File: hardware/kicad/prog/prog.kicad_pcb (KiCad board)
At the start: 4 copper layers, 174 x 134 mm, 144 parts, among them J1 AES_PROG, J2 Câble PROG-CHA, J3 CONF P, J4 CONF V, J5 microSD, SW1 Retour menu, U1 AMS1117-3.3, U10 iCE40HX4K-TQ144, U11 W9825G6KH-6, U12 iCE40HX4K-TQ144, U13 W9825G6KH-6, U2 AP2112K-1.2, U3 74LVC16244A, U4 74LVC16244A, U5 74LVC16244A, U6 74LVC16245A, U7 74LVC16245A, U8 74AHCT125, U9 74LVC1G07, X1 25 MHz 3,3 V, X2 25 MHz 3,3 V

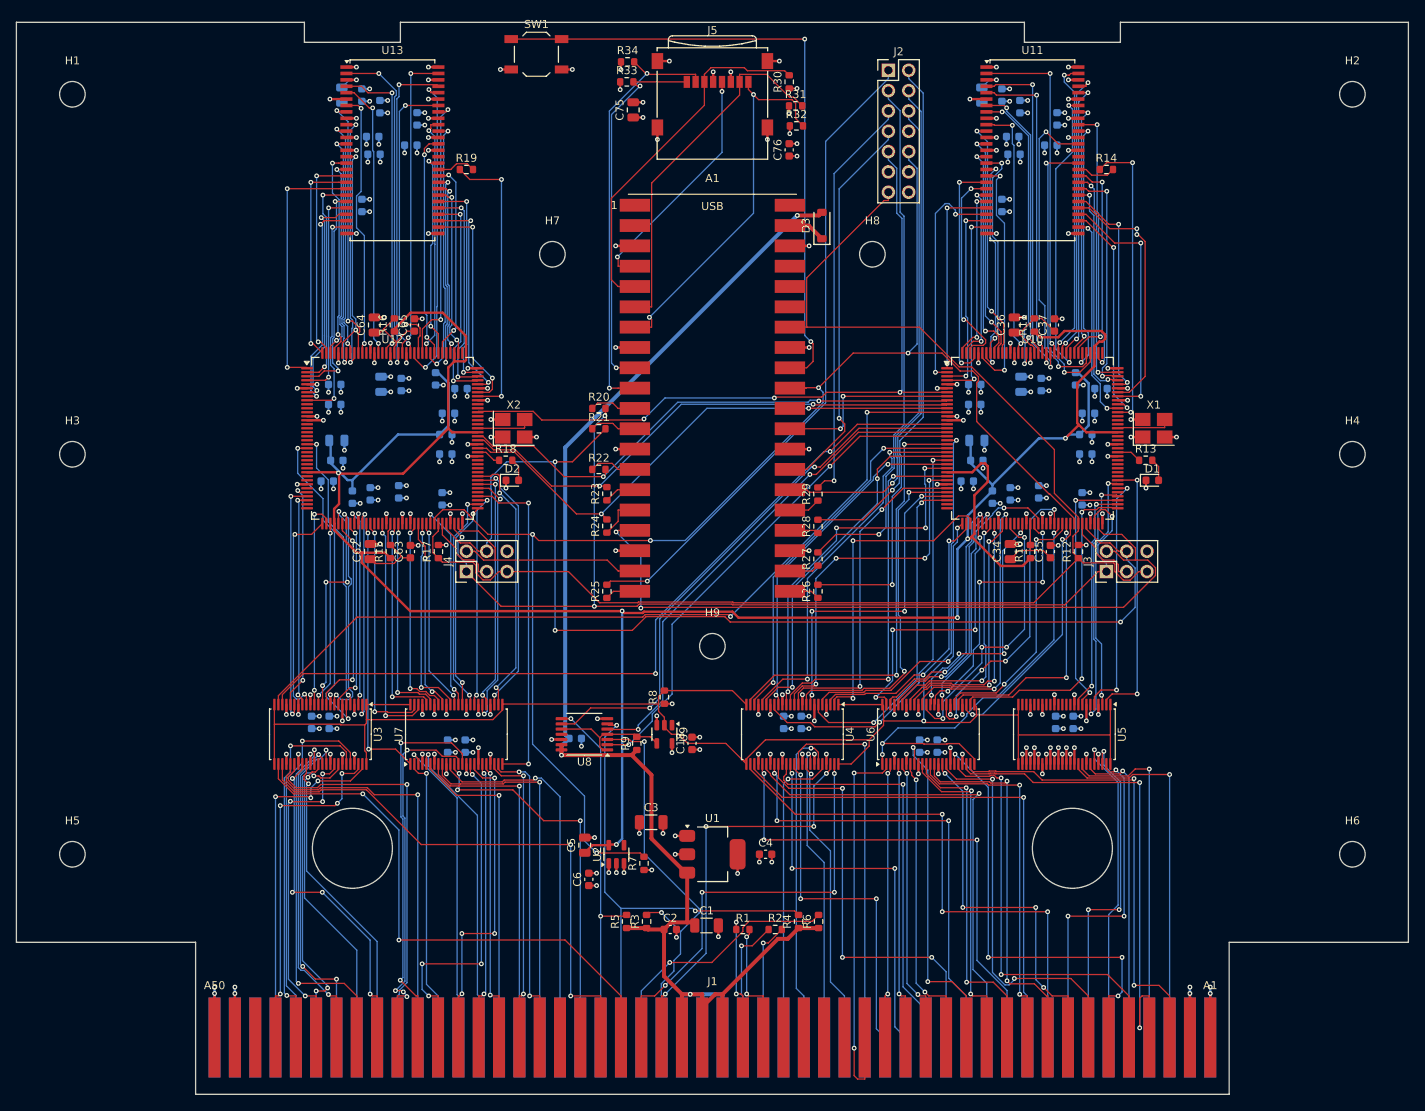
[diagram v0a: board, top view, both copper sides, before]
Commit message: Régulateur 3,3 V à découpage, horloge SDRAM adaptée côté FPGA, U8 en 74AHCT125
- AP63203 (TSOT-23-6, sortie fixe 3,3 V, ~90 %) à la place de
  l'AMS1117 : ~0,15 W de pertes au lieu de ~0,75 W et moins de courant
  tiré sur le 5 V de la console ; L 4,7 µH, Cin 10 µF, Cout 2 x 22 µF.
- Résistance série de 33 ohms de l'horloge SDRAM déclarée avec le FPGA :
  placée à 2,7 mm de sa broche (au lieu de ~30 mm, côté SDRAM).
- CHA : U8 (16244 pour 2 canaux) remplacé par un 74AHCT125.
Cartes replacées, contrôle Freerouting sans violation ; routage des
deux cartes et vérification de timing en cours.

Co-Authored-By: Claude Opus 5.5 <noreply@anthropic.com>
Claude-Session: https://claude.ai/code/session_01WKfXP1YJ8otGxZ5dsY6Agh
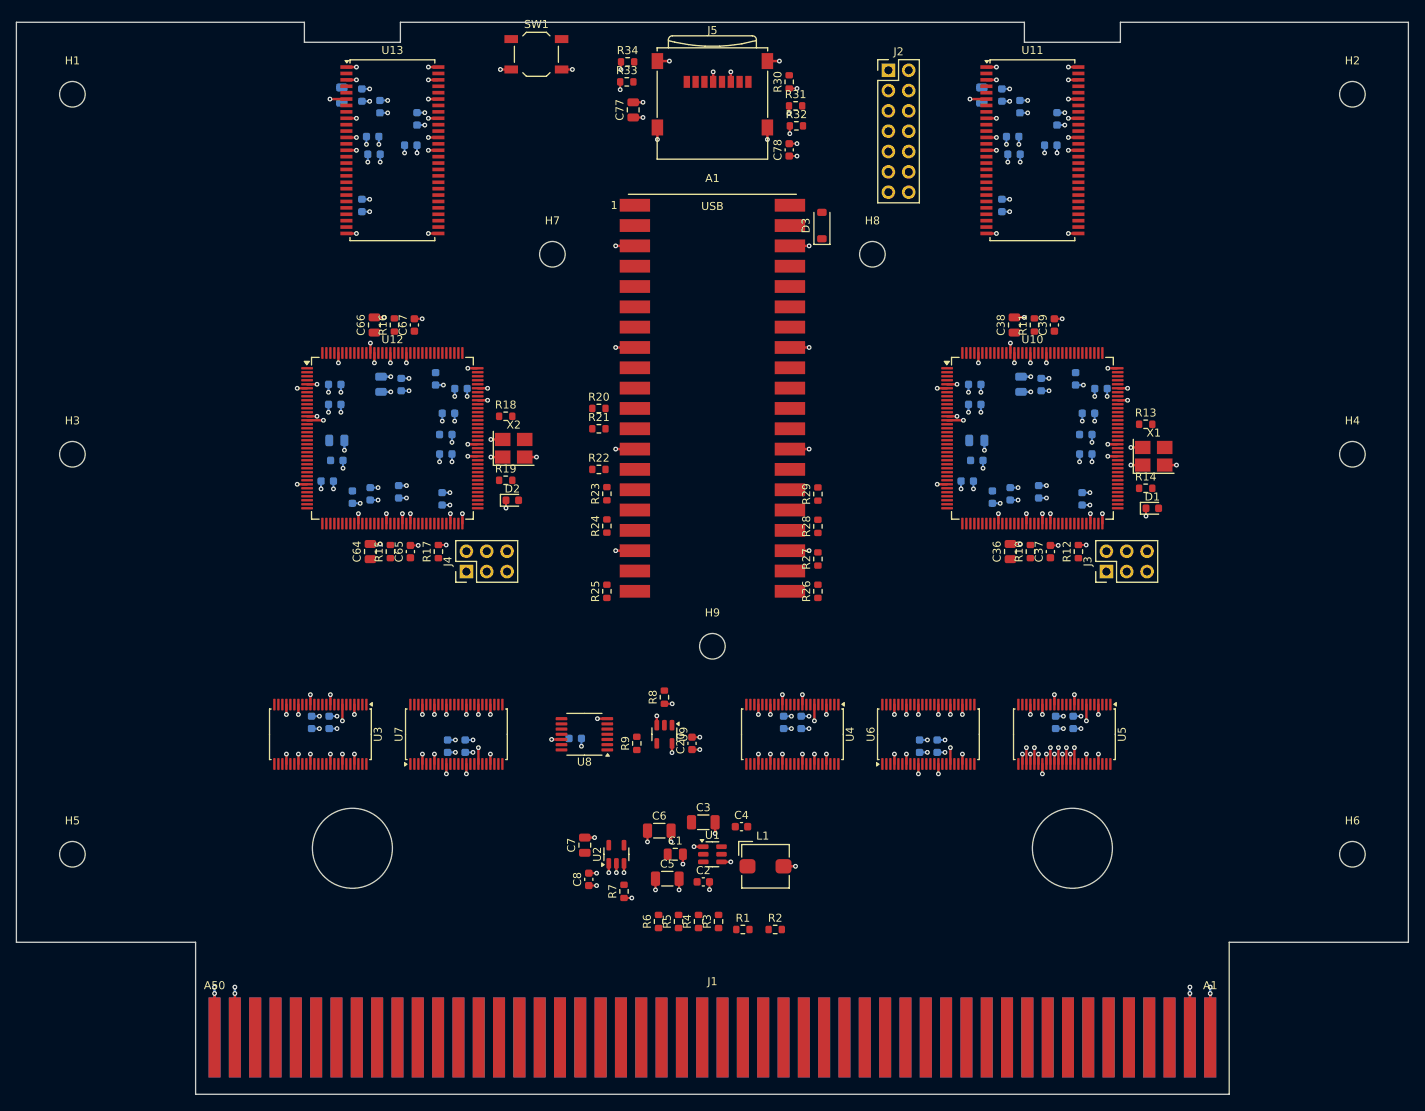
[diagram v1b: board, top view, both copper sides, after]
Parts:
- added C77: 10u, Capacitor_SMD:C_0805_2012Metric, F.Cu at (140.1, 57.0)
- added C78: 100n, Capacitor_SMD:C_0603_1608Metric, F.Cu at (159.6, 62.0)
- added L1: 4,7 µH 3 A, Inductor_SMD:L_Bourns_SRP5030T, F.Cu at (156.6, 151.5)
- C1: value 22u -> 10u; footprint Capacitor_SMD:C_1206_3216Metric -> Capacitor_SMD:C_0805_2012Metric
- C18: moved to B.Cu
- C20, C39, C67: moved to F.Cu
- C23, C33, C46, C51, C61, C74: value 10u -> 100n; footprint Capacitor_SMD:C_0805_2012Metric -> Capacitor_SMD:C_0603_1608Metric
- C25, C48, C53: value 100n -> 10u; footprint Capacitor_SMD:C_0603_1608Metric -> Capacitor_SMD:C_0805_2012Metric
- C34, C62, C75: value 10u -> 100n; footprint Capacitor_SMD:C_0805_2012Metric -> Capacitor_SMD:C_0603_1608Metric; moved to B.Cu
- C35, C63, C76: value 100n -> 10u; footprint Capacitor_SMD:C_0603_1608Metric -> Capacitor_SMD:C_0805_2012Metric; moved to B.Cu
- C38, C66, C7: value 100n -> 10u; footprint Capacitor_SMD:C_0603_1608Metric -> Capacitor_SMD:C_0805_2012Metric; moved to F.Cu
- C5: value 10u -> 22u; footprint Capacitor_SMD:C_0805_2012Metric -> Capacitor_SMD:C_1206_3216Metric
- C6: value 1u -> 22u; footprint Capacitor_SMD:C_0603_1608Metric -> Capacitor_SMD:C_1206_3216Metric
- C8: value 100n -> 1u; moved to F.Cu
- R13, R18: value 470 -> 33
- R14, R19: value 33 -> 470
- U1: value AMS1117-3.3 -> AP63203WU; footprint Package_TO_SOT_SMD:SOT-223-3_TabPin2 -> Package_TO_SOT_SMD:TSOT-23-6
- moved C47 99.6 mm to (193.1, 58.1), turned to -90 degrees
- moved C48 93.4 mm to (183.7, 55.1)
- moved C19 61.1 mm to (132.9, 135.5)
- moved C10 59.0 mm to (99.9, 133.5)
- moved C15 59.0 mm to (175.9, 136.5)
- moved C16 59.0 mm to (178.1, 136.5)
- moved C9 59.0 mm to (102.1, 133.5)
- moved C76 56.3 mm to (103.7, 55.1), turned to -90 degrees
- moved C20 48.6 mm to (147.4, 136.1), turned to 90 degrees
- moved R14 40.2 mm to (204.2, 104.2)
- moved C8 39.8 mm to (134.6, 153.1), turned to 90 degrees
- moved R19 39.2 mm to (124.2, 103.2)
- moved C7 35.4 mm to (134.1, 148.9), turned to 90 degrees
- moved C40 35.2 mm to (182.8, 91.3), turned to 0 degrees
- moved C68 35.2 mm to (102.8, 91.3), turned to 0 degrees
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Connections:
- C17 pad 1: +5V -> +3V3
- C19 pad 1: +1V2 -> +5V
- C20 pad 1: +1V2 -> +3V3
- C24 pad 1: +3V3 -> +1V2
- C25 pad 1: +3V3 -> +1V2
- C3 pad 1: +3V3 -> +5V
- C34 pad 1: P_VCCPLL0 -> +3V3
- C35 pad 1: P_VCCPLL0 -> +3V3
- C36 pad 1: P_VCCPLL1 -> P_VCCPLL0
- C37 pad 1: P_VCCPLL1 -> P_VCCPLL0
- C38 pad 1: +3V3 -> P_VCCPLL1
- C39 pad 1: +3V3 -> P_VCCPLL1
- C4 pad 1: +3V3 -> BST33
- C4 pad 2: GND -> SW33
- C47 pad 1: +1V2 -> +3V3
- C48 pad 1: +1V2 -> +3V3
- C5 pad 1: +1V2 -> +3V3
- C52 pad 1: +3V3 -> +1V2
- C53 pad 1: +3V3 -> +1V2
- C62 pad 1: V_VCCPLL0 -> +3V3
- C63 pad 1: V_VCCPLL0 -> +3V3
- C64 pad 1: V_VCCPLL1 -> V_VCCPLL0
- C65 pad 1: V_VCCPLL1 -> V_VCCPLL0
- C66 pad 1: +3V3 -> V_VCCPLL1
- C67 pad 1: +3V3 -> V_VCCPLL1
- C7 pad 1: +3V3 -> +1V2
- R13 pad 1: P_LED -> P_SD_CLK
- R13 pad 2: P_LED_K -> P_SD_CLK_R
- R14 pad 1: P_SD_CLK -> P_LED
- R14 pad 2: P_SD_CLK_R -> P_LED_K
- R18 pad 1: V_LED -> V_SD_CLK
- R18 pad 2: V_LED_K -> V_SD_CLK_R
- R19 pad 1: V_SD_CLK -> V_LED
- R19 pad 2: V_SD_CLK_R -> V_LED_K
- U1 pad 1: GND -> +3V3
- U1 pad 2: +3V3 -> +5V
- U10 pad 81: (no net) -> P_LED
- U10 pad 87: P_LED -> (no net)
- U10 pad 94: (no net) -> P_SD_CLK
- U10 pad 97: P_SD_CLK -> (no net)
- U12 pad 1: V_SD_BA0 -> V_SD_BA1
- U12 pad 101: V_SD_CLK -> V_SD_A4
- U12 pad 102: V_SD_A4 -> V_SD_A5
- U12 pad 104: V_SD_A5 -> V_SD_A6
- U12 pad 105: V_SD_A6 -> V_SD_A7
- U12 pad 106: V_SD_A7 -> V_SD_A8
- U12 pad 107: V_SD_A8 -> V_SD_A9
- U12 pad 110: V_SD_A9 -> V_SD_A11
- U12 pad 112: V_SD_A11 -> V_SD_A12
- U12 pad 113: V_SD_A12 -> V_SD_CKE
- U12 pad 114: V_SD_CKE -> V_SD_DQM1
- U12 pad 115: V_SD_DQM1 -> V_SD_DQ8
- U12 pad 116: V_SD_DQ8 -> V_SD_DQ9
- U12 pad 117: V_SD_DQ9 -> V_SD_DQ10
- U12 pad 118: V_SD_DQ10 -> V_SD_DQ11
- U12 pad 119: V_SD_DQ11 -> V_SD_DQ12
- U12 pad 120: V_SD_DQ12 -> V_SD_DQ13
- U12 pad 121: V_SD_DQ13 -> V_SD_DQ14
- U12 pad 122: V_SD_DQ14 -> V_SD_DQ15
- U12 pad 124: V_SD_DQ15 -> V_SD_DQ0
- U12 pad 125: V_SD_DQ0 -> V_SD_DQ1
- U12 pad 128: V_SD_DQ1 -> V_SD_DQ2
- U12 pad 130: V_SD_DQ2 -> V_SD_DQ3
- U12 pad 134: V_SD_DQ3 -> V_SD_DQ4
- U12 pad 135: V_SD_DQ4 -> V_SD_DQ5
- U12 pad 136: V_SD_DQ5 -> V_SD_DQ6
- U12 pad 137: V_SD_DQ6 -> V_SD_DQ7
- U12 pad 138: V_SD_DQ7 -> V_SD_DQM0
- U12 pad 139: V_SD_DQM0 -> V_SD_WE_N
- U12 pad 141: V_SD_WE_N -> V_SD_CAS_N
- U12 pad 142: V_SD_CAS_N -> V_SD_RAS_N
- U12 pad 143: V_SD_RAS_N -> V_SD_CS_N
- U12 pad 144: V_SD_CS_N -> V_SD_BA0
- U12 pad 2: V_SD_BA1 -> V_SD_A10
- U12 pad 3: V_SD_A10 -> V_SD_A0
- U12 pad 4: V_SD_A0 -> V_SD_A1
- U12 pad 7: V_SD_A1 -> V_SD_A2
- U12 pad 8: V_SD_A2 -> V_SD_A3
- U12 pad 84: (no net) -> V_LED
- U12 pad 87: V_LED -> (no net)
- U12 pad 9: V_SD_A3 -> (no net)
- U12 pad 96: (no net) -> V_SD_CLK
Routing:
- net +1V2: track 311.5 -> 0.00 mm, vias 6 -> 0
- net XLAT_EN_N: track 214.0 -> 0.00 mm, vias 2 -> 0
- net +5V: track 196.1 -> 0.00 mm, vias 3 -> 0
- net CDONE: track 186.1 -> 0.00 mm, vias 5 -> 0
- net CRESET_N: track 177.9 -> 0.00 mm
- net PROG_IO0: track 142.9 -> 0.00 mm, vias 3 -> 0
- net PROG_SCK: track 128.0 -> 0.00 mm, vias 4 -> 0
- net PORTWEU_N: track 104.5 -> 0.00 mm, vias 2 -> 0
- net PORTWEL_N: track 102.3 -> 0.00 mm, vias 2 -> 0
- net CS_P: track 95.0 -> 0.00 mm, vias 2 -> 0
- net MODE: track 91.5 -> 0.00 mm, vias 3 -> 0
- net CHA_SCK: track 81.6 -> 0.00 mm, vias 1 -> 0
- net BUTTON_N: track 80.6 -> 0.00 mm, vias 2 -> 0
- net CHA_IO0: track 76.1 -> 0.00 mm, vias 1 -> 0
- net AES_PORTWEL: track 69.4 -> 0.00 mm, vias 2 -> 0
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
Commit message: Carte PROG routée (régulateur à découpage, horloges SDRAM adaptées côté FPGA)
DRC : aucune liaison manquante, aucune violation de cuivre.

Co-Authored-By: Claude Opus 5.5 <noreply@anthropic.com>
Claude-Session: https://claude.ai/code/session_01WKfXP1YJ8otGxZ5dsY6Agh
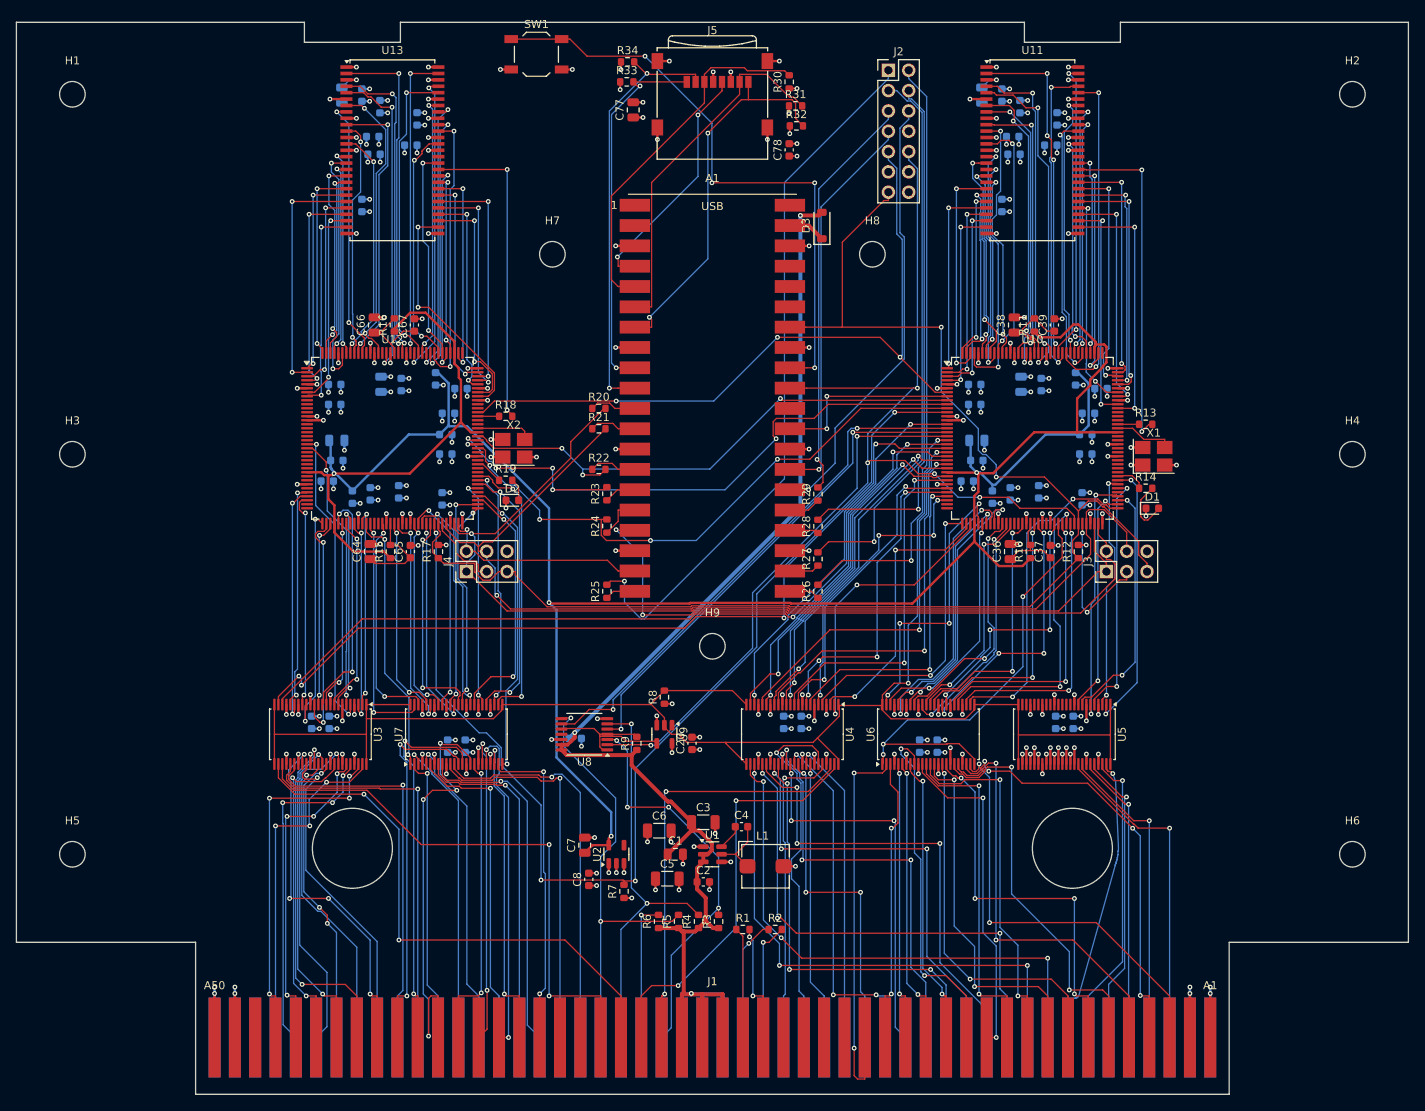
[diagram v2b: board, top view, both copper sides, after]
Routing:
- net +1V2: track 0.00 -> 309.8 mm, vias 0 -> 4
- net CDONE: track 0.00 -> 215.2 mm, vias 0 -> 7
- net XLAT_EN_N: track 0.00 -> 208.2 mm, vias 0 -> 2
- net CRESET_N: track 0.00 -> 185.2 mm, vias 0 -> 2
- net +5V: track 0.00 -> 185.2 mm, vias 0 -> 3
- net PROG_IO0: track 0.00 -> 127.3 mm, vias 0 -> 1
- net PROG_SCK: track 0.00 -> 123.9 mm, vias 0 -> 1
- net PORTWEU_N: track 0.00 -> 107.8 mm, vias 0 -> 4
- net PORTWEL_N: track 0.00 -> 103.8 mm, vias 0 -> 2
- net MODE: track 0.00 -> 91.9 mm, vias 0 -> 3
- net CHA_SCK: track 0.00 -> 89.6 mm, vias 0 -> 1
- net CS_P: track 0.00 -> 83.5 mm, vias 0 -> 2
- net PROG_IO2: track 0.00 -> 78.8 mm, vias 0 -> 5
- net BUTTON_N: track 0.00 -> 76.0 mm, vias 0 -> 4
- net CHA_IO0: track 0.00 -> 75.9 mm, vias 0 -> 1
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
